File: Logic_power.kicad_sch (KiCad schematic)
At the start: 11 parts, among them U10 TPS54202DDC, U2 XC6206P332MR-G

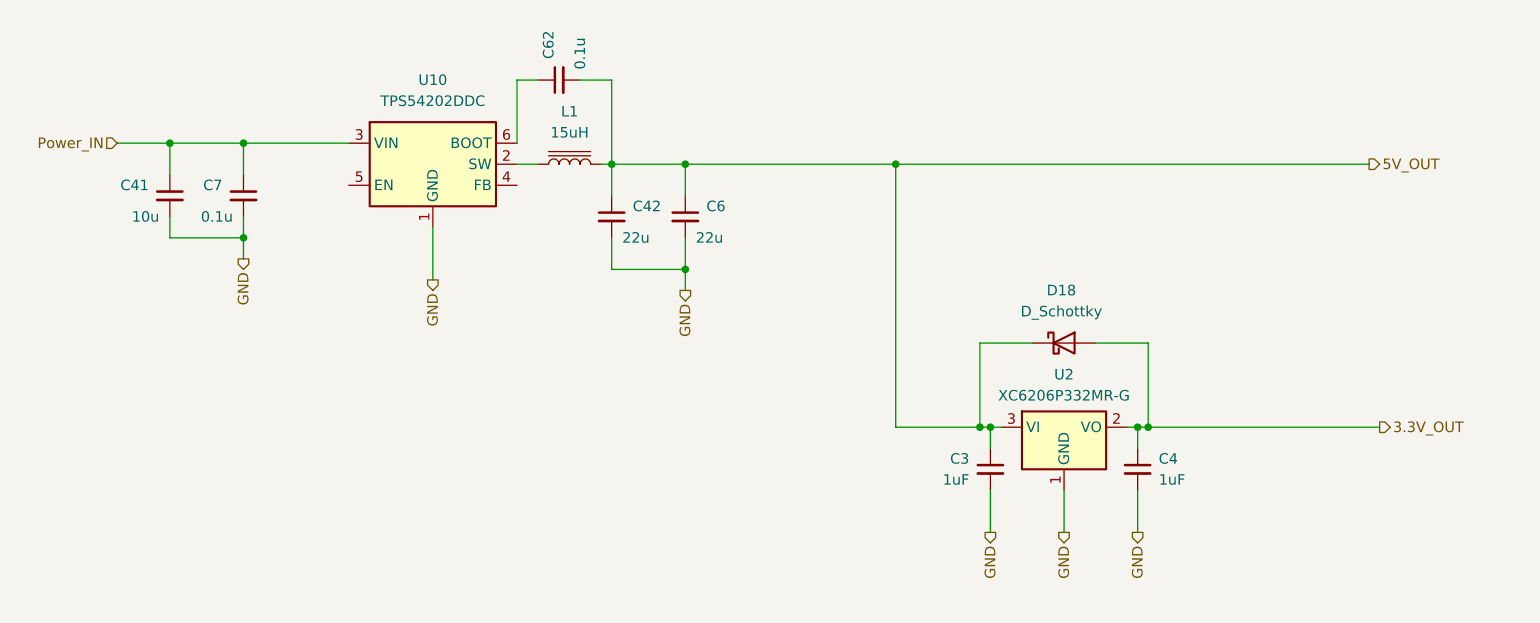
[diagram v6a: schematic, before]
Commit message: Update PCB design & add microSD connector
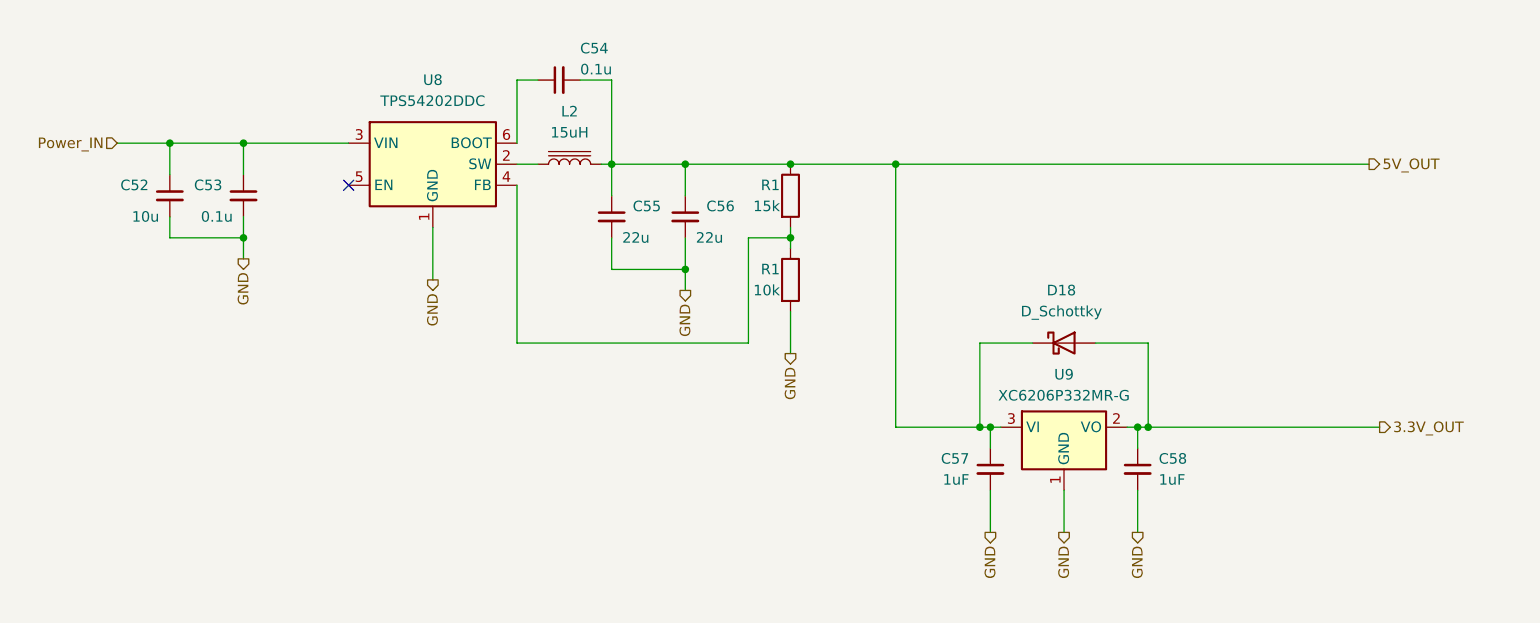
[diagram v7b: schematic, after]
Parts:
- added R1: 10k, Resistor_SMD:R_0603_1608Metric, symbol Device:R
- added R1: 15k, Resistor_SMD:R_0603_1608Metric, symbol Device:R
- C52: renamed from C41; footprint Capacitor_SMD:C_0603_1608Metric_Pad1.08x0.95mm_HandSolder -> Capacitor_SMD:C_0603_1608Metric
- C53: renamed from C7; footprint Capacitor_SMD:C_0603_1608Metric_Pad1.08x0.95mm_HandSolder -> Capacitor_SMD:C_0603_1608Metric
- C54: renamed from C62; footprint Capacitor_SMD:C_0603_1608Metric_Pad1.08x0.95mm_HandSolder -> Capacitor_SMD:C_0603_1608Metric
- C55: renamed from C42; footprint Capacitor_SMD:C_0603_1608Metric_Pad1.08x0.95mm_HandSolder -> Capacitor_SMD:C_0603_1608Metric
- C56: renamed from C6; footprint Capacitor_SMD:C_0603_1608Metric_Pad1.08x0.95mm_HandSolder -> Capacitor_SMD:C_0603_1608Metric
- C57: renamed from C3; footprint Capacitor_SMD:C_0603_1608Metric_Pad1.08x0.95mm_HandSolder -> Capacitor_SMD:C_0603_1608Metric
- C58: renamed from C4; footprint Capacitor_SMD:C_0603_1608Metric_Pad1.08x0.95mm_HandSolder -> Capacitor_SMD:C_0603_1608Metric
- renumbered L1 to L2, U10 to U8, U2 to U9
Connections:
- net 5V_OUT: now also R1.1
- net GND: now also R1.2
- net at U8.4 (FB): now also R1.1, R1.2
- no-connect marks 0 -> 1

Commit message: change logic DCDC
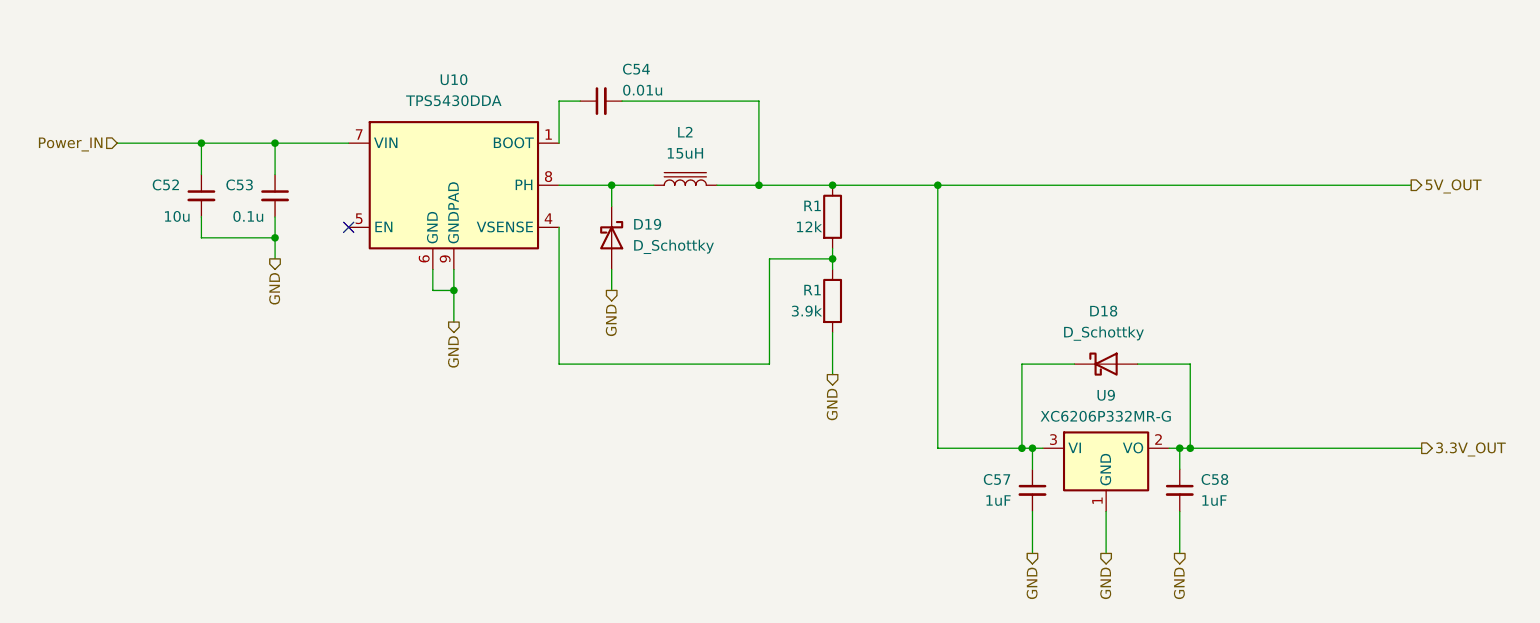
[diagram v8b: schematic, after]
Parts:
- removed C55, C56: 22u, Capacitor_SMD:C_0603_1608Metric, symbol Device:C_Small
- removed U8: TPS54202DDC, Package_TO_SOT_SMD:SOT-23-6, symbol Regulator_Switching:TPS54202DDC
- added D19: D_Schottky, Diode_SMD:D_SOD-123F, symbol Device:D_Schottky
- added U10: TPS5430DDA, Package_SO:TI_SO-PowerPAD-8_ThermalVias, symbol Regulator_Switching:TPS5430DDA
- C54: value 0.1u -> 0.01u
- R1: value 10k -> 3.9k
- R1: value 15k -> 12k
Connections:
- net GND: now also D19.2 (A), U10.6 (GND), U10.9 (GNDPAD)
- net Power_IN: now also U10.7 (VIN)
- net at C54.1: now also U10.1 (BOOT)
- net at L2.1: now also D19.1 (K), U10.8 (PH)
- net at R1.1, R1.2: now also U10.4 (VSENSE)
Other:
- moved on the sheet: C52, C53, C54, C57, C58, D18, L2, R1, U9
